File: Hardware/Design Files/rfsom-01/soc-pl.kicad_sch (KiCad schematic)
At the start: 2 parts

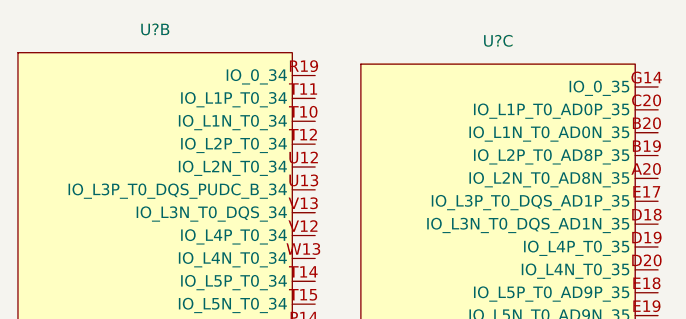
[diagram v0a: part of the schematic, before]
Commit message: ddr progress; added more conns;
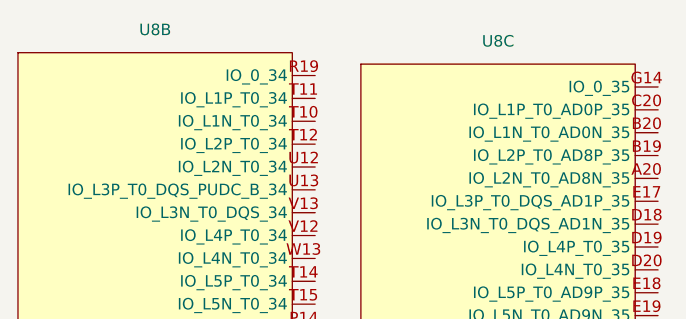
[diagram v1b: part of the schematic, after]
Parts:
- U8: renamed from U?; footprint Package_BGA:Xilinx_CLG400 -> ICs:CLG400
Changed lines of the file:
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@@
 		(dnp no)
 		(fields_autoplaced yes)
-		(property "Reference" "U?"
+		(property "Reference" "U8"
 			(at 80.01 30.48 0)
 			(effects
@@
 			)
 		)
-		(property "Footprint" "Package_BGA:Xilinx_CLG400"
+		(property "Footprint" "ICs:CLG400"
 			(at 64.77 33.02 0)
 			(effects
@@
 			(project "rfsom-01"
 				(path "/5dade83d-850c-4336-8f49-e0e8e6ebca37/01ce84f5-9c7a-43d2-9b5a-4d08cbdcd7ae/dcd4ebf5-9bf5-4a13-8e67-04058a43970d"
-					(reference "U?")
+					(reference "U8")
 					(unit 2)
 				)
@@
 		(dnp no)
 		(fields_autoplaced yes)
-		(property "Reference" "U?"
+		(property "Reference" "U8"
 			(at 118.11 31.75 0)
 			(effects
@@
 			)
 		)
-		(property "Footprint" "Package_BGA:Xilinx_CLG400"
+		(property "Footprint" "ICs:CLG400"
 			(at 102.87 34.29 0)
 			(effects
@@
 			(project "rfsom-01"
 				(path "/5dade83d-850c-4336-8f49-e0e8e6ebca37/01ce84f5-9c7a-43d2-9b5a-4d08cbdcd7ae/dcd4ebf5-9bf5-4a13-8e67-04058a43970d"
-					(reference "U?")
+					(reference "U8")
 					(unit 3)
 				)

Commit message: ps progress; added ftdi; mezz pinout pedinging;
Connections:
- net AD8-: now reaches U8.A20 (IO_L2N_T0_AD8N_35)
- net AD8+: now reaches U8.B19 (IO_L2P_T0_AD8P_35)
- net AD0-: now reaches U8.B20 (IO_L1N_T0_AD0N_35)
- net AD0+: now reaches U8.C20 (IO_L1P_T0_AD0P_35)
- net AD12+: now reaches U8.F19 (IO_L15P_T2_DQS_AD12P_35)
- net AD12-: now reaches U8.F20 (IO_L15N_T2_DQS_AD12N_35)
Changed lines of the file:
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@@
 	(generator_version "9.0")
 	(paper "A4")
+	(wire
+		(pts
+			(xy 151.13 46.99) (xy 135.89 46.99)
+		)
+		(stroke
+			(width 0)
+			(type default)
+		)
+	)
+	(wire
+		(pts
+			(xy 151.13 113.03) (xy 135.89 113.03)
+		)
+		(stroke
+			(width 0)
+			(type default)
+		)
+	)
+	(wire
+		(pts
+			(xy 151.13 44.45) (xy 135.89 44.45)
+		)
+		(stroke
+			(width 0)
+			(type default)
+		)
+	)
+	(wire
+		(pts
+			(xy 151.13 41.91) (xy 135.89 41.91)
+		)
+		(stroke
+			(width 0)
+			(type default)
+		)
+	)
+	(wire
+		(pts
+			(xy 151.13 110.49) (xy 135.89 110.49)
+		)
+		(stroke
+			(width 0)
+			(type default)
+		)
+	)
+	(wire
+		(pts
+			(xy 151.13 39.37) (xy 135.89 39.37)
+		)
+		(stroke
+			(width 0)
+			(type default)
+		)
+	)
+	(label "AD12-"
+		(at 151.13 113.03 180)
+		(effects
+			(font
+				(size 1.27 1.27)
+			)
+			(justify right bottom)
+		)
+	)
+	(label "AD8+"
+		(at 151.13 44.45 180)
+		(effects
+			(font
+				(size 1.27 1.27)
+			)
+			(justify right bottom)
+		)
+	)
+	(label "AD0+"
+		(at 151.13 39.37 180)
+		(effects
+			(font
+				(size 1.27 1.27)
+			)
+			(justify right bottom)
+		)
+	)
+	(label "AD12+"
+		(at 151.13 110.49 180)
+		(effects
+			(font
+				(size 1.27 1.27)
+			)
+			(justify right bottom)
+		)
+	)
+	(label "AD0-"
+		(at 151.13 41.91 180)
+		(effects
+			(font
+				(size 1.27 1.27)
+			)
+			(justify right bottom)
+		)
+	)
+	(label "AD8-"
+		(at 151.13 46.99 180)
+		(effects
+			(font
+				(size 1.27 1.27)
+			)
+			(justify right bottom)
+		)
+	)
 	(symbol
 		(lib_id "ICs:XC7Z010-1CLG400C")

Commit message: some ddr routing progress; layerstack per pcbway standard options, review reqd; commit prior to ddr split;
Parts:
- renumbered U8 to U5
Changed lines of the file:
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@@
 		(dnp no)
 		(fields_autoplaced yes)
-		(property "Reference" "U8"
+		(property "Reference" "U5"
 			(at 80.01 30.48 0)
 			(effects
@@
 		(instances
 			(project "rfsom-01"
-				(path "/5dade83d-850c-4336-8f49-e0e8e6ebca37/01ce84f5-9c7a-43d2-9b5a-4d08cbdcd7ae/dcd4ebf5-9bf5-4a13-8e67-04058a43970d"
-					(reference "U8")
+				(path "/5dade83d-850c-4336-8f49-e0e8e6ebca37/5824b29f-0639-4332-9093-651d63d89232/dcd4ebf5-9bf5-4a13-8e67-04058a43970d"
+					(reference "U5")
 					(unit 2)
 				)
@@
 		(dnp no)
 		(fields_autoplaced yes)
-		(property "Reference" "U8"
+		(property "Reference" "U5"
 			(at 118.11 31.75 0)
 			(effects
@@
 		(instances
 			(project "rfsom-01"
-				(path "/5dade83d-850c-4336-8f49-e0e8e6ebca37/01ce84f5-9c7a-43d2-9b5a-4d08cbdcd7ae/dcd4ebf5-9bf5-4a13-8e67-04058a43970d"
-					(reference "U8")
+				(path "/5dade83d-850c-4336-8f49-e0e8e6ebca37/5824b29f-0639-4332-9093-651d63d89232/dcd4ebf5-9bf5-4a13-8e67-04058a43970d"
+					(reference "U5")
 					(unit 3)
 				)

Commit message: added starage, usb sch; more design progress in sch;
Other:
- added sheet ram-pl (ram.kicad_sch)
- moved on the sheet: U5B, U5C

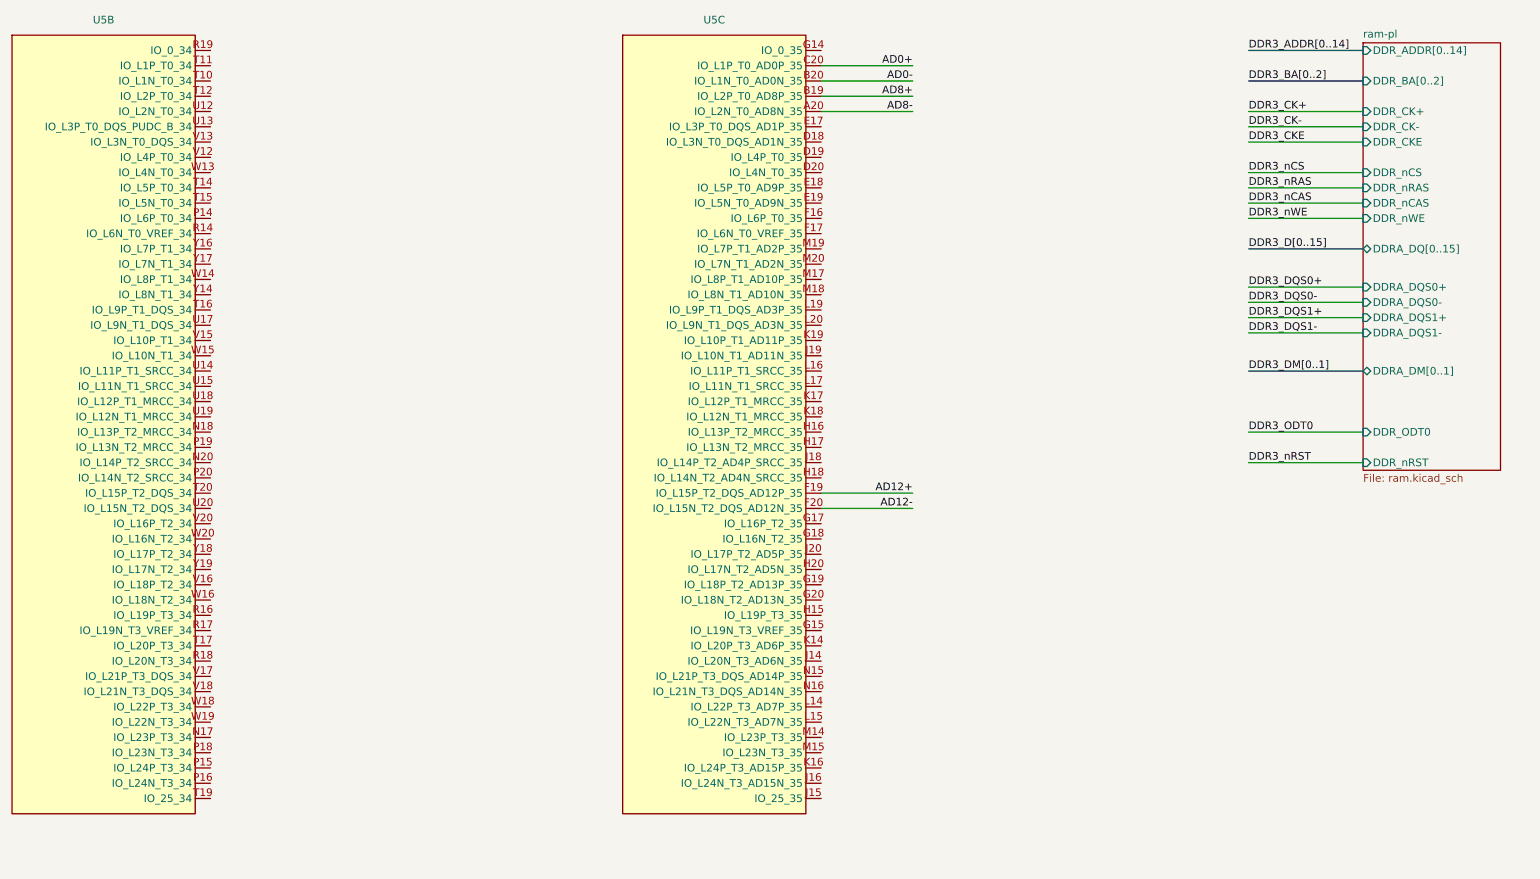
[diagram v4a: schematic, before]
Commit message: routing changes; added mezzanine; added pl ram;
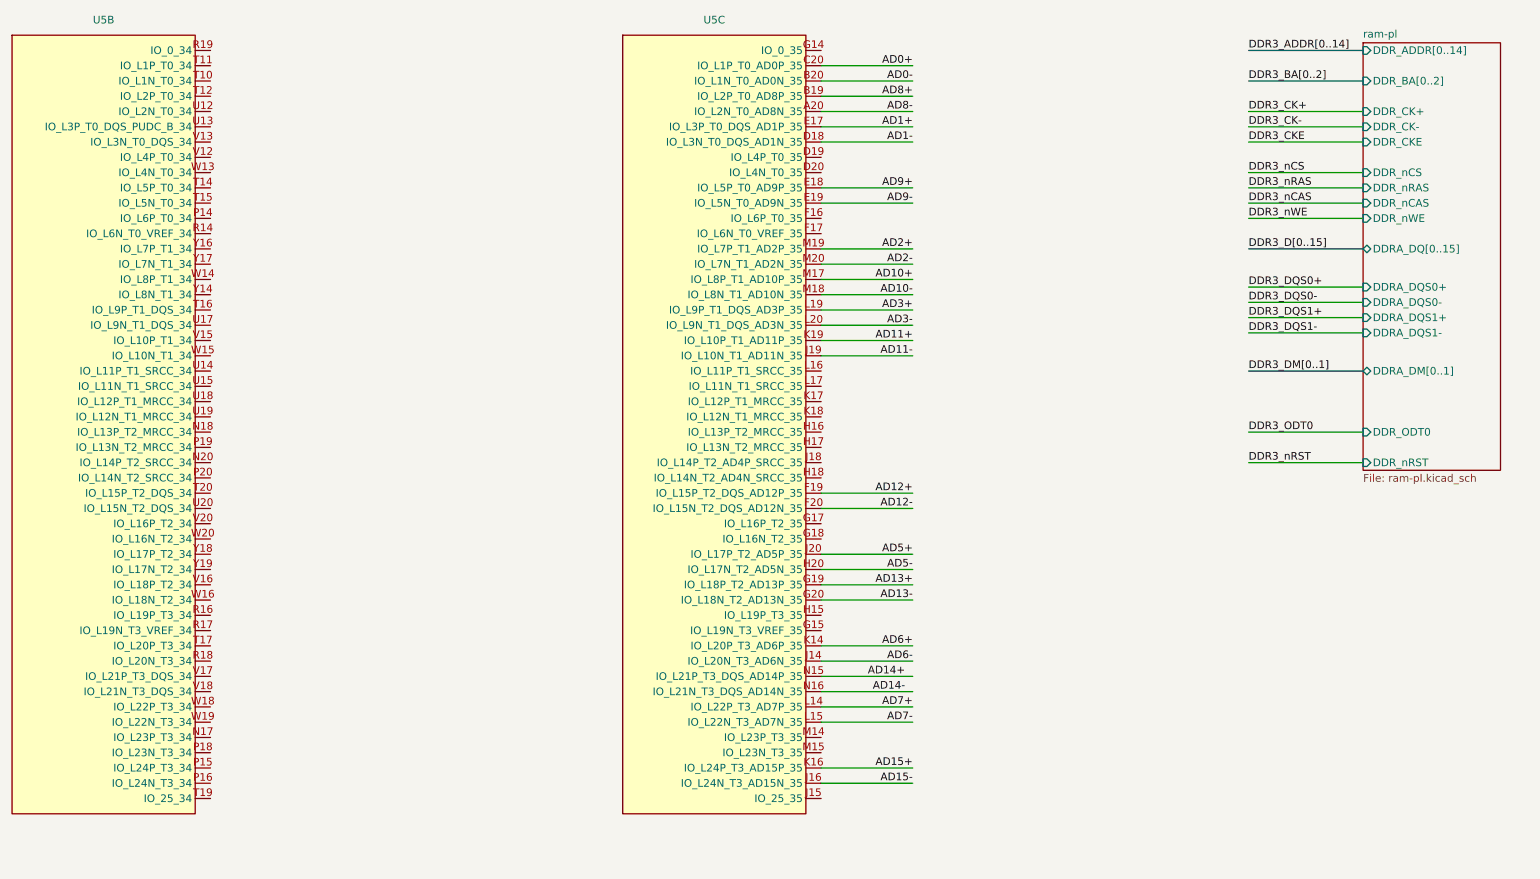
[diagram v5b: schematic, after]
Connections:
- net AD1-: now reaches U5.D18 (IO_L3N_T0_DQS_AD1N_35)
- net AD1+: now reaches U5.E17 (IO_L3P_T0_DQS_AD1P_35)
- net AD9+: now reaches U5.E18 (IO_L5P_T0_AD9P_35)
- net AD9-: now reaches U5.E19 (IO_L5N_T0_AD9N_35)
- net AD13+: now reaches U5.G19 (IO_L18P_T2_AD13P_35)
- net AD13-: now reaches U5.G20 (IO_L18N_T2_AD13N_35)
- net AD5-: now reaches U5.H20 (IO_L17N_T2_AD5N_35)
- net AD6-: now reaches U5.J14 (IO_L20N_T3_AD6N_35)
- net AD15-: now reaches U5.J16 (IO_L24N_T3_AD15N_35)
- net AD11-: now reaches U5.J19 (IO_L10N_T1_AD11N_35)
- net AD5+: now reaches U5.J20 (IO_L17P_T2_AD5P_35)
- net AD6+: now reaches U5.K14 (IO_L20P_T3_AD6P_35)
- net AD15+: now reaches U5.K16 (IO_L24P_T3_AD15P_35)
- net AD11+: now reaches U5.K19 (IO_L10P_T1_AD11P_35)
- net AD7+: now reaches U5.L14 (IO_L22P_T3_AD7P_35)
- net AD7-: now reaches U5.L15 (IO_L22N_T3_AD7N_35)
- net AD3+: now reaches U5.L19 (IO_L9P_T1_DQS_AD3P_35)
- net AD3-: now reaches U5.L20 (IO_L9N_T1_DQS_AD3N_35)
- net AD10+: now reaches U5.M17 (IO_L8P_T1_AD10P_35)
- net AD10-: now reaches U5.M18 (IO_L8N_T1_AD10N_35)
- net AD2+: now reaches U5.M19 (IO_L7P_T1_AD2P_35)
- net AD2-: now reaches U5.M20 (IO_L7N_T1_AD2N_35)
- net AD14+: now reaches U5.N15 (IO_L21P_T3_DQS_AD14P_35)
- net AD14-: now reaches U5.N16 (IO_L21N_T3_DQS_AD14N_35)
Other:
- sheet ram-pl: file ram.kicad_sch -> ram-pl.kicad_sch

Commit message: updated sch pdf; routign progress;
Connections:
- net DDR3_CK+: now also U5.V20 (IO_L16P_T2_34)
- net DDR3_CK-: now also U5.W20 (IO_L16N_T2_34)
- net DDR3_CKE: now also U5.R16 (IO_L19P_T3_34)
- net DDR3_DQS0+: now also U5.U13 (IO_L3P_T0_DQS_PUDC_B_34)
- net DDR3_DQS0-: now also U5.V13 (IO_L3N_T0_DQS_34)
- net DDR3_DQS1+: now also U5.V12 (IO_L4P_T0_34)
- net DDR3_DQS1-: now also U5.W13 (IO_L4N_T0_34)
- net DDR3_ODT0: now also U5.R18 (IO_L20N_T3_34)
- net DDR3_nCAS: now also U5.Y19 (IO_L17N_T2_34)
- net DDR3_nCS: now also U5.T17 (IO_L20P_T3_34)
- net DDR3_nRAS: now also U5.Y18 (IO_L17P_T2_34)
- net DDR3_nRST: now also U5.W16 (IO_L18N_T2_34)
- net DDR3_nWE: now also U5.V16 (IO_L18P_T2_34)
- net DDR3_D12: now reaches U5.N17 (IO_L23P_T3_34)
- net DDR3_ADDR14: now reaches U5.N18 (IO_L13P_T2_MRCC_34)
- net DDR3_BA1: now reaches U5.N20 (IO_L14P_T2_SRCC_34)
- net DDR3_ADDR0: now reaches U5.P14 (IO_L6P_T0_34)
- net DDR3_D14: now reaches U5.P15 (IO_L24P_T3_34)
- net DDR3_D15: now reaches U5.P16 (IO_L24N_T3_34)
- net DDR3_D13: now reaches U5.P18 (IO_L23N_T3_34)
- net DDR3_D5: now reaches U5.P19 (IO_L13N_T2_MRCC_34)
- net DDR3_BA2: now reaches U5.P20 (IO_L14N_T2_SRCC_34)
- net DDR3_ADDR1: now reaches U5.R14 (IO_L6N_T0_VREF_34)
- net DDR3_D7: now reaches U5.R17 (IO_L19N_T3_VREF_34)
- net DDR3_D0: now reaches U5.R19 (IO_0_34)
- net DDR3_D2: now reaches U5.T10 (IO_L1N_T0_34)
- net DDR3_D1: now reaches U5.T11 (IO_L1P_T0_34)
- net DDR3_D3: now reaches U5.T12 (IO_L2P_T0_34)
- net DDR3_DM0: now reaches U5.T14 (IO_L5P_T0_34)
- net DDR3_DM1: now reaches U5.T15 (IO_L5N_T0_34)
- net DDR3_ADDR6: now reaches U5.T16 (IO_L9P_T1_DQS_34)
- net DDR3_D6: now reaches U5.T20 (IO_L15P_T2_DQS_34)
- net DDR3_D4: now reaches U5.U12 (IO_L2N_T0_34)
- net DDR3_ADDR10: now reaches U5.U14 (IO_L11P_T1_SRCC_34)
- net DDR3_ADDR11: now reaches U5.U15 (IO_L11N_T1_SRCC_34)
- net DDR3_ADDR7: now reaches U5.U17 (IO_L9N_T1_DQS_34)
- net DDR3_ADDR12: now reaches U5.U18 (IO_L12P_T1_MRCC_34)
- net DDR3_ADDR13: now reaches U5.U19 (IO_L12N_T1_MRCC_34)
- net DDR3_BA0: now reaches U5.U20 (IO_L15N_T2_DQS_34)
- net DDR3_ADDR8: now reaches U5.V15 (IO_L10P_T1_34)
- net DDR3_D8: now reaches U5.V17 (IO_L21P_T3_DQS_34)
- net DDR3_D9: now reaches U5.V18 (IO_L21N_T3_DQS_34)
- net DDR3_ADDR4: now reaches U5.W14 (IO_L8P_T1_34)
- net DDR3_ADDR9: now reaches U5.W15 (IO_L10N_T1_34)
- net DDR3_D10: now reaches U5.W18 (IO_L22P_T3_34)
- net DDR3_D11: now reaches U5.W19 (IO_L22N_T3_34)
- net DDR3_ADDR5: now reaches U5.Y14 (IO_L8N_T1_34)
- net DDR3_ADDR2: now reaches U5.Y16 (IO_L7P_T1_34)
- net DDR3_ADDR3: now reaches U5.Y17 (IO_L7N_T1_34)
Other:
- sheet ram-pl ports: added DDR_DM[0..1], DDR_DQS0+, DDR_DQS0-, DDR_DQS1+, DDR_DQS1-, DDR_DQ[0..15]; removed DDRA_DM[0..1], DDRA_DQS0+, DDRA_DQS0-, DDRA_DQS1+, DDRA_DQS1-, DDRA_DQ[0..15]
